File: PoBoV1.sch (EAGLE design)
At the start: 77 parts, among them IC1 INA232, Q1 IPZ40N04S5L-4R8, Q2 IPZ40N04S5L-4R8, U1 TPS55288RPMR, X1 +Vin, X18 OUT, X19 ADDRSEL, X3 SDA, X4 SCL, X5 VOUT/EXT, X6 FB SEL, X7 EN SEL, X8 MODE SEL

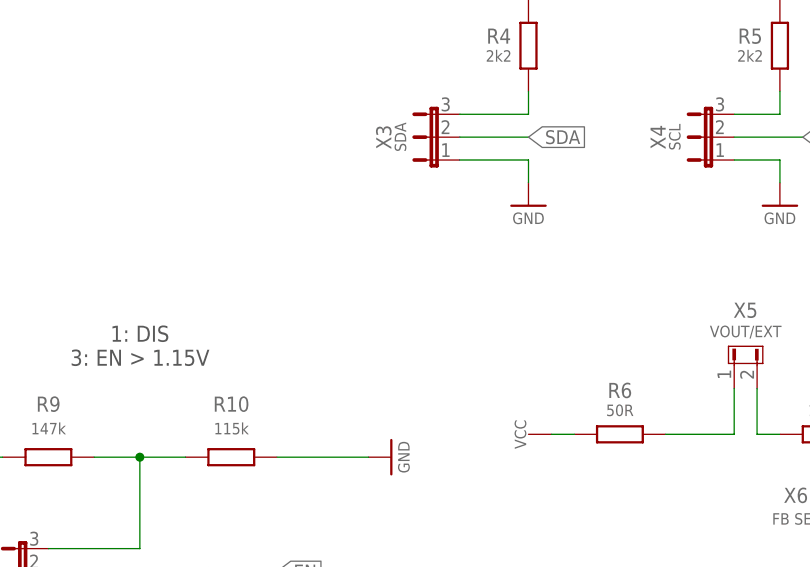
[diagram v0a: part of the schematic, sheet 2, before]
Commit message: Made some traces thiccer and added bananaplug
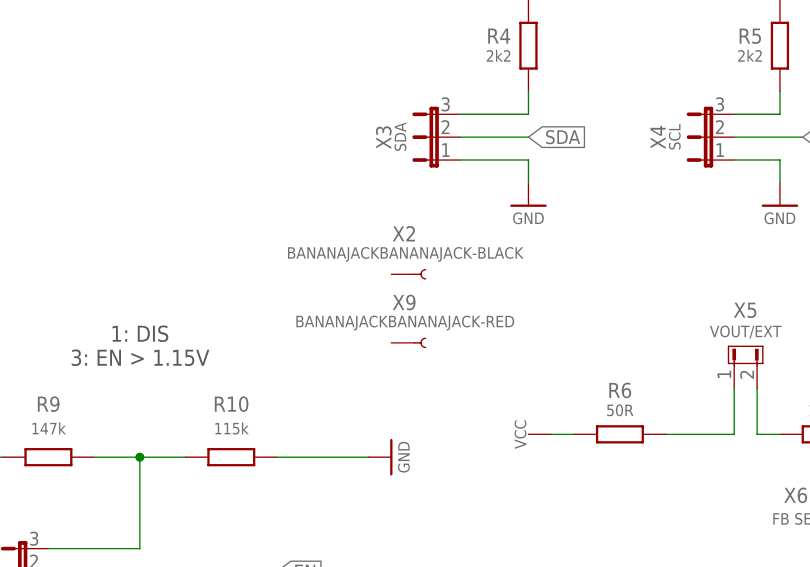
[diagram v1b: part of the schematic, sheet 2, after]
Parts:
- added X2: BANANAJACKBANANAJACK-BLACK, con_PoeD:BANANAJACKBANANAJACK-BLACK
- added X9: BANANAJACKBANANAJACK-RED, con_PoeD:BANANAJACKBANANAJACK-RED
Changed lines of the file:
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@@
 <part name="P+47" library="supply_STRH" deviceset="PGND" device=""/>
 <part name="F1" library="fuse_SekS" library_urn="urn:adsk.eagle:library:37507069" deviceset="TE5" device="" package3d_urn="urn:adsk.eagle:package:39521299/3" value="4A"/>
+<part name="X2" library="con_PoeD" library_urn="urn:adsk.eagle:library:37347325" deviceset="BANANAJACK" device="BANANAJACK-BLACK" package3d_urn="urn:adsk.eagle:package:40115465/7"/>
+<part name="X9" library="con_PoeD" library_urn="urn:adsk.eagle:library:37347325" deviceset="BANANAJACK" device="BANANAJACK-RED" package3d_urn="urn:adsk.eagle:package:40115465/7"/>
 </parts>
 <sheets>
@@
 <attribute name="VALUE" x="251.968" y="48.768" size="1.27" layer="96"/>
 </instance>
+<instance part="X2" gate="G$1" x="172.72" y="124.46" smashed="yes">
+<attribute name="NAME" x="174.19" y="128.11" size="1.6764" layer="95" font="vector" align="bottom-center"/>
+<attribute name="VALUE" x="174.24" y="126.198" size="1.27" layer="96" font="vector" align="bottom-center"/>
+</instance>
+<instance part="X9" gate="G$1" x="172.72" y="116.84" smashed="yes">
+<attribute name="NAME" x="174.19" y="120.49" size="1.6764" layer="95" font="vector" align="bottom-center"/>
+<attribute name="VALUE" x="174.24" y="118.578" size="1.27" layer="96" font="vector" align="bottom-center"/>
+</instance>
 </instances>

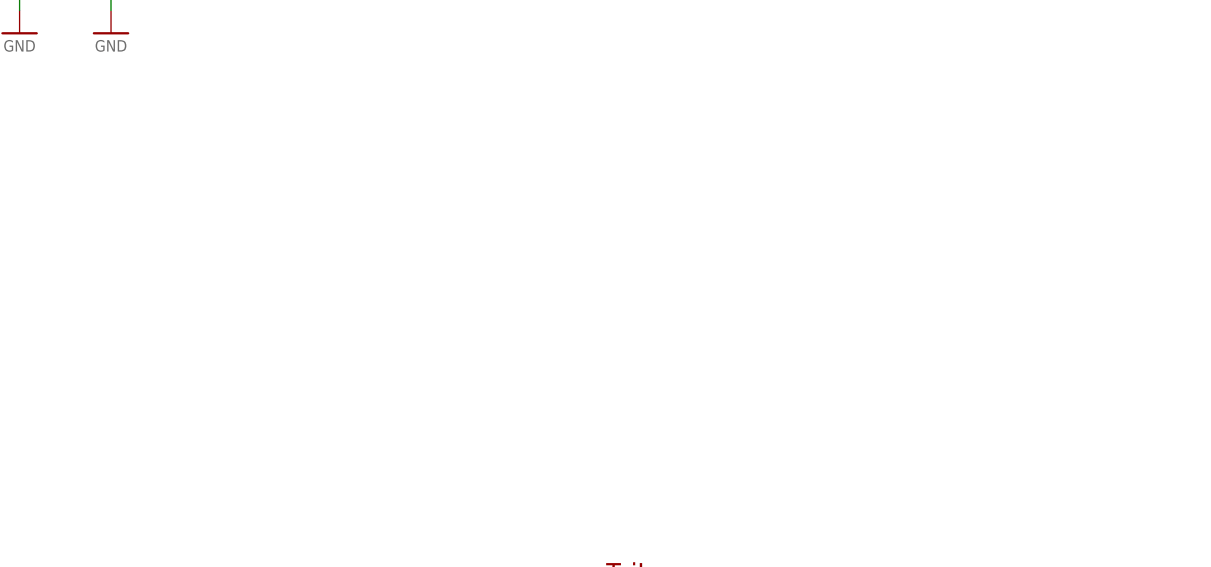
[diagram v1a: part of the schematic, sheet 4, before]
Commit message: Add files via upload
Added testpoints and banana jacks
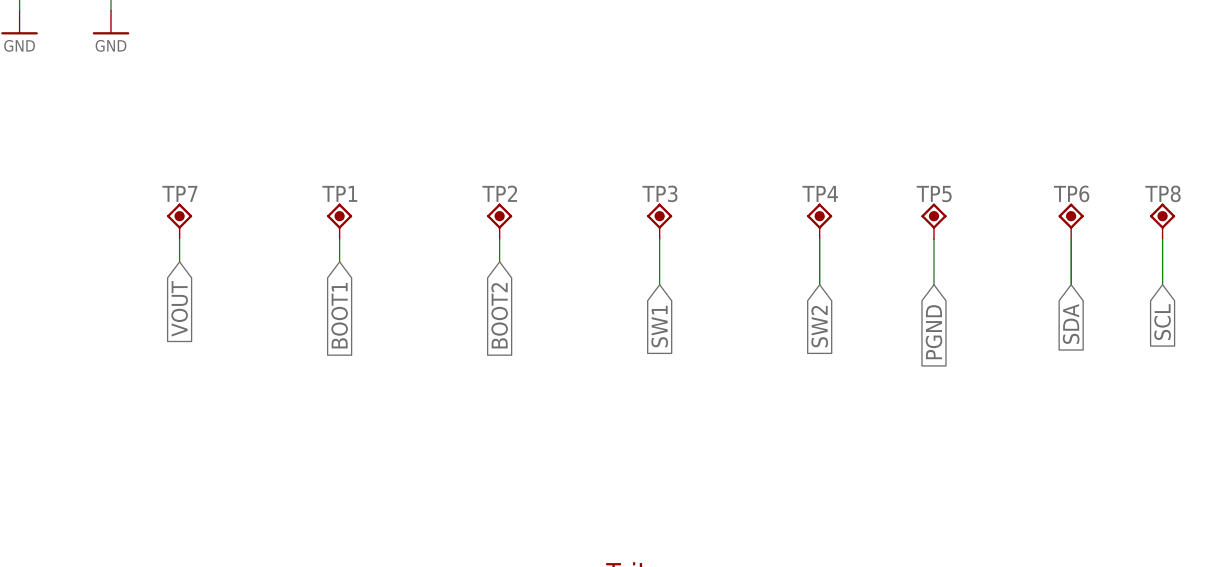
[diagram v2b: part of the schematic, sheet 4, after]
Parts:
- removed X18: OUT, con_SekS:AK500/2
- added TP1, TP2, TP3, TP4, TP5, TP6, TP7, TP8: TPP-SMD-20SN, testpoint:TPP-SMD-20SN
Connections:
- removed net N$21: IC1.IN-, R20.1, X18-2.KL
- new net VOUT: IC1.IN-, R20.1, TP7.P, X9.2
- net BOOT1: now also TP1.P
- net BOOT2: now also TP2.P
- net PGND: now also TP5.P, X2.2; no longer X18-1.KL
- net SCL: now also TP8.P
- net SDA: now also TP6.P
- net SW1: now also TP3.P
- net SW2: now also TP4.P
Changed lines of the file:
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@@
 <setting verticaltext="up"/>
 </settings>
-<grid distance="0.1" unitdist="inch" unit="inch" style="lines" multiple="1" display="no" altdistance="0.01" altunitdist="inch" altunit="inch"/>
+<grid distance="0.1" unitdist="inch" unit="inch" style="lines" multiple="1" display="yes" altdistance="0.01" altunitdist="inch" altunit="inch"/>
 <layers>
 <layer number="1" name="Top" color="4" fill="1" visible="no" active="no"/>
@@
 <part name="C28" library="RPoettinger" deviceset="C-EU" device="C0805" package3d_urn="urn:adsk.eagle:package:14147459/1" value="1u"/>
 <part name="P+24" library="supply_STRH" deviceset="PGND" device=""/>
-<part name="X18" library="con_SekS" library_urn="urn:adsk.eagle:library:37507037" deviceset="AK500/2" device="" package3d_urn="urn:adsk.eagle:package:38663950/2" value="OUT"/>
 <part name="FRAMES1" library="frames_SekS_V22" library_urn="urn:adsk.eagle:library:37507199" deviceset="HTL-A4Q-V22" device=""/>
 <part name="FRAMES2" library="frames_SekS_V22" library_urn="urn:adsk.eagle:library:37507199" deviceset="HTL-A4Q-V22" device=""/>
@@
 <part name="X2" library="con_PoeD" library_urn="urn:adsk.eagle:library:37347325" deviceset="BANANAJACK" device="BANANAJACK-BLACK" package3d_urn="urn:adsk.eagle:package:40115465/7"/>
 <part name="X9" library="con_PoeD" library_urn="urn:adsk.eagle:library:37347325" deviceset="BANANAJACK" device="BANANAJACK-RED" package3d_urn="urn:adsk.eagle:package:40115465/7"/>
+<part name="TP1" library="testpoint" deviceset="TPP" device="-SMD-20SN"/>
+<part name="TP2" library="testpoint" deviceset="TPP" device="-SMD-20SN"/>
+<part name="TP3" library="testpoint" deviceset="TPP" device="-SMD-20SN"/>
+<part name="TP4" library="testpoint" deviceset="TPP" device="-SMD-20SN"/>
+<part name="TP5" library="testpoint" deviceset="TPP" device="-SMD-20SN"/>
+<part name="TP6" library="testpoint" deviceset="TPP" device="-SMD-20SN"/>
+<part name="TP7" library="testpoint" deviceset="TPP" device="-SMD-20SN"/>
+<part name="TP8" library="testpoint" deviceset="TPP" device="-SMD-20SN"/>
 </parts>
 <sheets>
@@
 <attribute name="VALUE" x="251.968" y="48.768" size="1.27" layer="96"/>
 </instance>
-<instance part="X2" gate="G$1" x="172.72" y="124.46" smashed="yes">
-<attribute name="NAME" x="174.19" y="128.11" size="1.6764" layer="95" font="vector" align="bottom-center"/>
-<attribute name="VALUE" x="174.24" y="126.198" size="1.27" layer="96" font="vector" align="bottom-center"/>
-</instance>
-<instance part="X9" gate="G$1" x="172.72" y="116.84" smashed="yes">
-<attribute name="NAME" x="174.19" y="120.49" size="1.6764" layer="95" font="vector" align="bottom-center"/>
-<attribute name="VALUE" x="174.24" y="118.578" size="1.27" layer="96" font="vector" align="bottom-center"/>
-</instance>
 </instances>
 <busses>
@@
 <attribute name="VALUE" x="127" y="84.328" size="1.27" layer="96" font="vector" align="bottom-center"/>
 </instance>
+<instance part="TP1" gate="G$1" x="175.26" y="66.04" smashed="yes">
+<attribute name="NAME" x="173.355" y="67.6275" size="1.778" layer="95"/>
+</instance>
+<instance part="TP2" gate="G$1" x="193.04" y="66.04" smashed="yes">
+<attribute name="NAME" x="191.135" y="67.6275" size="1.778" layer="95"/>
+</instance>
+<instance part="TP3" gate="G$1" x="210.82" y="66.04" smashed="yes">
+<attribute name="NAME" x="208.915" y="67.6275" size="1.778" layer="95"/>
+</instance>
+<instance part="TP4" gate="G$1" x="228.6" y="66.04" smashed="yes">
+<attribute name="NAME" x="226.695" y="67.6275" size="1.778" layer="95"/>
+</instance>
+<instance part="TP5" gate="G$1" x="241.3" y="66.04" smashed="yes">
+<attribute name="NAME" x="239.395" y="67.6275" size="1.778" layer="95"/>
+</instance>
+<instance part="TP6" gate="G$1" x="256.54" y="66.04" smashed="yes">
+<attribute name="NAME" x="254.635" y="67.6275" size="1.778" layer="95"/>
+</instance>
+<instance part="TP7" gate="G$1" x="157.48" y="66.04" smashed="yes">
+<attribute name="NAME" x="155.575" y="67.6275" size="1.778" layer="95"/>
+</instance>
+<instance part="TP8" gate="G$1" x="266.7" y="66.04" smashed="yes">
+<attribute name="NAME" x="264.795" y="67.6275" size="1.778" layer="95"/>
+</instance>
 </instances>
 <busses>
@@
 <label x="78.74" y="127" size="1.27" layer="95" rot="R180" xref="yes"/>
 </segment>
+<segment>
+<pinref part="TP6" gate="G$1" pin="P"/>
+<wire x1="256.54" y1="63.5" x2="256.54" y2="58.42" width="0.1524" layer="91"/>
+<label x="256.54" y="58.42" size="1.778" layer="95" rot="R270" xref="yes"/>
+</segment>
 </net>
 <net name="SCL" class="0">
@@
 <label x="78.74" y="129.54" size="1.27" layer="95" rot="R180" xref="yes"/>
 </segment>
+<segment>
+<pinref part="TP8" gate="G$1" pin="P"/>
+<wire x1="266.7" y1="63.5" x2="266.7" y2="58.42" width="0.1524" layer="91"/>
+<label x="266.7" y="58.42" size="1.778" layer="95" rot="R270" xref="yes"/>
+</segment>
 </net>
 <net name="PGND" class="0">
@@
 <wire x1="246.38" y1="132.08" x2="246.38" y2="127" width="0.1524" layer="91"/>
 <pinref part="P+26" gate="G$1" pin="PGND"/>
+</segment>
+<segment>
+<pinref part="TP5" gate="G$1" pin="P"/>
+<wire x1="241.3" y1="63.5" x2="241.3" y2="58.42" width="0.1524" layer="91"/>
+<label x="241.3" y="58.42" size="1.778" layer="95" rot="R270" xref="yes"/>
 </segment>
 </net>
@@
 <wire x1="121.92" y1="121.92" x2="129.54" y2="121.92" width="0.1524" layer="91"/>
 </segment>
+<segment>
+<pinref part="TP2" gate="G$1" pin="P"/>
+<wire x1="193.04" y1="63.5" x2="193.04" y2="60.96" width="0.1524" layer="91"/>
+<label x="193.04" y="60.96" size="1.778" layer="95" rot="R270" xref="yes"/>
+</segment>
 </net>
 <net name="BOOT1" class="0">
@@
 <wire x1="121.92" y1="124.46" x2="129.54" y2="124.46" width="0.1524" layer="91"/>
 <label x="129.54" y="124.46" size="1.27" layer="95" xref="yes"/>
+</segment>
+<segment>
+<pinref part="TP1" gate="G$1" pin="P"/>
+<wire x1="175.26" y1="63.5" x2="175.26" y2="60.96" width="0.1524" layer="91"/>
+<label x="175.26" y="60.96" size="1.778" layer="95" rot="R270" xref="yes"/>
 </segment>
 </net>
@@
 <label x="129.54" y="114.3" size="1.27" layer="95" xref="yes"/>
 </segment>
+<segment>
+<pinref part="TP4" gate="G$1" pin="P"/>
+<wire x1="228.6" y1="63.5" x2="228.6" y2="58.42" width="0.1524" layer="91"/>
+<label x="228.6" y="58.42" size="1.778" layer="95" rot="R270" xref="yes"/>
+</segment>
 </net>
 <net name="SW1" class="0">
@@
 <wire x1="121.92" y1="116.84" x2="129.54" y2="116.84" width="0.1524" layer="91"/>
 <label x="129.54" y="116.84" size="1.27" layer="95" xref="yes"/>
+</segment>
+<segment>
+<pinref part="TP3" gate="G$1" pin="P"/>
+<wire x1="210.82" y1="63.5" x2="210.82" y2="58.42" width="0.1524" layer="91"/>
+<label x="210.82" y="58.42" size="1.778" layer="95" rot="R270" xref="yes"/>
 </segment>
 </net>
@@
 <wire x1="160.02" y1="142.24" x2="160.02" y2="137.16" width="0.1524" layer="91"/>
 <label x="160.02" y="142.24" size="1.27" layer="95" xref="yes"/>
+</segment>
+</net>
+<net name="VOUT" class="0">
+<segment>
+<pinref part="TP7" gate="G$1" pin="P"/>
+<wire x1="157.48" y1="63.5" x2="157.48" y2="60.96" width="0.1524" layer="91"/>
+<label x="157.48" y="60.96" size="1.778" layer="95" rot="R270" xref="yes"/>
 </segment>
 </net>
@@
 <attribute name="VALUE" x="119.888" y="89.408" size="1.27" layer="96"/>
 </instance>
-<instance part="X18" gate="-1" x="175.26" y="83.82" smashed="yes" rot="R180"/>
-<instance part="X18" gate="-2" x="175.26" y="99.06" smashed="yes" rot="R180">
-<attribute name="NAME" x="172.72" y="90.805" size="1.6764" layer="95" font="vector" rot="MR0" align="bottom-center"/>
-<attribute name="VALUE" x="172.72" y="88.011" size="1.27" layer="96" font="vector" align="bottom-center"/>
-</instance>
 <instance part="C29" gate="G$1" x="27.94" y="104.14" smashed="yes">
 <attribute name="NAME" x="33.02" y="102.3366" size="1.6764" layer="95" font="vector" align="bottom-center"/>
@@
 <instance part="GND13" gate="1" x="190.5" y="78.74" smashed="yes">
 <attribute name="VALUE" x="190.5" y="76.962" size="1.27" layer="96" font="vector" align="bottom-center"/>
+</instance>
+<instance part="X2" gate="G$1" x="172.72" y="86.36" smashed="yes">
+<attribute name="NAME" x="174.19" y="90.01" size="1.6764" layer="95" font="vector" align="bottom-center"/>
+<attribute name="VALUE" x="174.24" y="88.098" size="1.27" layer="96" font="vector" align="bottom-center"/>
+</instance>
+<instance part="X9" gate="G$1" x="172.72" y="96.52" smashed="yes">
+<attribute name="NAME" x="174.19" y="100.17" size="1.6764" layer="95" font="vector" align="bottom-center"/>
+<attribute name="VALUE" x="174.24" y="98.258" size="1.27" layer="96" font="vector" align="bottom-center"/>
 </instance>
 </instances>
@@
 </segment>
 <segment>
-<pinref part="X18" gate="-1" pin="KL"/>
-<wire x1="172.72" y1="83.82" x2="172.72" y2="78.74" width="0.1524" layer="91"/>
+<wire x1="172.72" y1="86.36" x2="172.72" y2="78.74" width="0.1524" layer="91"/>
 <pinref part="P+42" gate="G$1" pin="PGND"/>
+<pinref part="X2" gate="G$1" pin="2"/>
 </segment>
 </net>
@@
 </segment>
 </net>
-<net name="N$21" class="0">
+<net name="VOUT" class="0">
 <segment>
 <pinref part="R20" gate="G$1" pin="1"/>
-<pinref part="X18" gate="-2" pin="KL"/>
-<wire x1="172.72" y1="104.14" x2="172.72" y2="99.06" width="0.1524" layer="91"/>
+<wire x1="172.72" y1="104.14" x2="172.72" y2="96.52" width="0.1524" layer="91"/>
 <wire x1="172.72" y1="104.14" x2="185.42" y2="104.14" width="0.1524" layer="91"/>
 <junction x="172.72" y="104.14"/>
@@
 <pinref part="IC1" gate="G$1" pin="IN-"/>
 <wire x1="185.42" y1="111.76" x2="198.12" y2="111.76" width="0.1524" layer="91"/>
-</segment>
-</net>
+<pinref part="X9" gate="G$1" pin="2"/>
+<label x="162.56" y="104.14" size="1.27" layer="95" rot="R180" xref="yes"/>
+<wire x1="172.72" y1="104.14" x2="162.56" y2="104.14" width="0.1524" layer="91"/>
+</segment>
+</net>
